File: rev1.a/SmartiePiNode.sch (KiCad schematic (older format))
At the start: 53 parts, among them CN1 USBMICROb, CN2 ST-LINK, CN3 SX1238_TRX_HEADER, SW1 SW_PUSH, U1 ISL91127IR, U2 STM32L052_LQFP48, X1 abm10, X2 ABS25-32.768KHZ-6-T

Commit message: more schematic/usb verification.
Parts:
- added R?: 1.5K, symbol R_Small
- added R?: 100K, Resistors_SMD:R_0603, symbol R_Small
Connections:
- net +3V3: now also R?.1
- net GND: now also R?.1
- net at CN1.3 (D+), R3.2: now also R?.2
- net at CN1.4 (NC): now also R?.2
- no-connect marks 3 -> 2
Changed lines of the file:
@@
 $EndComp
 $Comp
-L GND #PWR10
+L GND #PWR01
 U 1 1 5B041A53
 P 3720 7315
-F 0 "#PWR10" H 3720 7065 50  0001 C CNN
+F 0 "#PWR01" H 3720 7065 50  0001 C CNN
 F 1 "GND" H 3725 7142 50  0000 C CNN
 F 2 "" H 3720 7315 50  0001 C CNN
@@
 $EndComp
 $Comp
-L GND #PWR15
+L GND #PWR02
 U 1 1 5B041F18
 P 4975 6485
-F 0 "#PWR15" H 4975 6235 50  0001 C CNN
+F 0 "#PWR02" H 4975 6235 50  0001 C CNN
 F 1 "GND" H 4980 6312 50  0000 C CNN
 F 2 "" H 4975 6485 50  0001 C CNN
@@
 $EndComp
 $Comp
-L GND #PWR16
+L GND #PWR03
 U 1 1 5B04234F
 P 5255 6485
-F 0 "#PWR16" H 5255 6235 50  0001 C CNN
+F 0 "#PWR03" H 5255 6235 50  0001 C CNN
 F 1 "GND" H 5260 6312 50  0000 C CNN
 F 2 "" H 5255 6485 50  0001 C CNN
@@
 $EndComp
 $Comp
-L GND #PWR17
+L GND #PWR04
 U 1 1 5B0423C8
 P 5530 6485
-F 0 "#PWR17" H 5530 6235 50  0001 C CNN
+F 0 "#PWR04" H 5530 6235 50  0001 C CNN
 F 1 "GND" H 5535 6312 50  0000 C CNN
 F 2 "" H 5530 6485 50  0001 C CNN
@@
 $EndComp
 $Comp
-L GND #PWR6
+L GND #PWR05
 U 1 1 5B04306E
 P 2340 6485
-F 0 "#PWR6" H 2340 6235 50  0001 C CNN
+F 0 "#PWR05" H 2340 6235 50  0001 C CNN
 F 1 "GND" H 2345 6312 50  0000 C CNN
 F 2 "" H 2340 6485 50  0001 C CNN
@@
 $EndComp
 $Comp
-L GND #PWR4
+L GND #PWR06
 U 1 1 5B04307C
 P 2060 6485
-F 0 "#PWR4" H 2060 6235 50  0001 C CNN
+F 0 "#PWR06" H 2060 6235 50  0001 C CNN
 F 1 "GND" H 2065 6312 50  0000 C CNN
 F 2 "" H 2060 6485 50  0001 C CNN
@@
 $EndComp
 $Comp
-L GND #PWR3
+L GND #PWR07
 U 1 1 5B04308A
 P 1785 6485
-F 0 "#PWR3" H 1785 6235 50  0001 C CNN
+F 0 "#PWR07" H 1785 6235 50  0001 C CNN
 F 1 "GND" H 1790 6312 50  0000 C CNN
 F 2 "" H 1785 6485 50  0001 C CNN
@@
 $EndComp
 $Comp
-L GND #PWR7
+L GND #PWR08
 U 1 1 5B043F5D
 P 2705 7280
-F 0 "#PWR7" H 2705 7030 50  0001 C CNN
+F 0 "#PWR08" H 2705 7030 50  0001 C CNN
 F 1 "GND" H 2710 7107 50  0000 C CNN
 F 2 "" H 2705 7280 50  0001 C CNN
@@
 $EndComp
 $Comp
-L GND #PWR12
+L GND #PWR09
 U 1 1 5B044D4C
 P 4485 7315
-F 0 "#PWR12" H 4485 7065 50  0001 C CNN
+F 0 "#PWR09" H 4485 7065 50  0001 C CNN
 F 1 "GND" H 4490 7142 50  0000 C CNN
 F 2 "" H 4485 7315 50  0001 C CNN
@@
 $EndComp
 $Comp
-L GND #PWR22
+L GND #PWR010
 U 1 1 5B06F6EF
 P 9930 3790
-F 0 "#PWR22" H 9930 3540 50  0001 C CNN
+F 0 "#PWR010" H 9930 3540 50  0001 C CNN
 F 1 "GND" H 9935 3617 50  0000 C CNN
 F 2 "" H 9930 3790 50  0001 C CNN
@@
 $EndComp
 $Comp
-L GND #PWR20
+L GND #PWR011
 U 1 1 5B0753BB
 P 6760 3380
-F 0 "#PWR20" H 6760 3130 50  0001 C CNN
+F 0 "#PWR011" H 6760 3130 50  0001 C CNN
 F 1 "GND" H 6765 3207 50  0000 C CNN
 F 2 "" H 6760 3380 50  0001 C CNN
@@
 	0    1    1    0
 $EndComp
-NoConn ~ 1465 4560
-$Comp
-L GND #PWR1
+$Comp
+L GND #PWR012
 U 1 1 5B081C3A
-P 1545 4710
-F 0 "#PWR1" H 1545 4460 50  0001 C CNN
-F 1 "GND" H 1550 4537 50  0000 C CNN
-F 2 "" H 1545 4710 50  0001 C CNN
-F 3 "" H 1545 4710 50  0001 C CNN
-	1    1545 4710
+P 1715 4725
+F 0 "#PWR012" H 1715 4475 50  0001 C CNN
+F 1 "GND" H 1720 4552 50  0000 C CNN
+F 2 "" H 1715 4725 50  0001 C CNN
+F 3 "" H 1715 4725 50  0001 C CNN
+	1    1715 4725
 	1    0    0    -1
 $EndComp
@@
 $EndComp
 $Comp
-L GND #PWR18
+L GND #PWR013
 U 1 1 5B082DC4
 P 5880 3240
-F 0 "#PWR18" H 5880 2990 50  0001 C CNN
+F 0 "#PWR013" H 5880 2990 50  0001 C CNN
 F 1 "GND" H 5885 3067 50  0000 C CNN
 F 2 "" H 5880 3240 50  0001 C CNN
@@
 	1465 4260 1895 4260
 Wire Wire Line
-	1545 4660 1545 4710
-Wire Wire Line
-	1465 4660 1545 4660
-Wire Wire Line
 	1465 4460 1850 4460
 Wire Wire Line
@@
 Connection ~ 10575 2935
 $Comp
-L GND #PWR23
+L GND #PWR014
 U 1 1 5B098D9A
 P 11070 2830
-F 0 "#PWR23" H 11070 2580 50  0001 C CNN
+F 0 "#PWR014" H 11070 2580 50  0001 C CNN
 F 1 "GND" H 11075 2657 50  0000 C CNN
 F 2 "" H 11070 2830 50  0001 C CNN
@@
 	2225 1540 2225 1670
 $Comp
-L GND #PWR5
+L GND #PWR015
 U 1 1 5B0A5E1E
 P 2225 1670
-F 0 "#PWR5" H 2225 1420 50  0001 C CNN
+F 0 "#PWR015" H 2225 1420 50  0001 C CNN
 F 1 "GND" H 2230 1497 50  0000 C CNN
 F 2 "" H 2225 1670 50  0001 C CNN
@@
 +3V3
 $Comp
-L GND #PWR8
+L GND #PWR016
 U 1 1 5B0AC996
 P 3070 1200
-F 0 "#PWR8" H 3070 950 50  0001 C CNN
+F 0 "#PWR016" H 3070 950 50  0001 C CNN
 F 1 "GND" H 3075 1027 50  0000 C CNN
 F 2 "" H 3070 1200 50  0001 C CNN
@@
 SPI2_SCK
 $Comp
-L GND #PWR9
+L GND #PWR017
 U 1 1 5B0AE690
 P 3070 1500
-F 0 "#PWR9" H 3070 1250 50  0001 C CNN
+F 0 "#PWR017" H 3070 1250 50  0001 C CNN
 F 1 "GND" H 3075 1327 50  0000 C CNN
 F 2 "" H 3070 1500 50  0001 C CNN
@@
 	4145 2100 4720 2100
 $Comp
-L GND #PWR13
+L GND #PWR018
 U 1 1 5B0AEB87
 P 4720 2100
-F 0 "#PWR13" H 4720 1850 50  0001 C CNN
+F 0 "#PWR018" H 4720 1850 50  0001 C CNN
 F 1 "GND" H 4725 1927 50  0000 C CNN
 F 2 "" H 4720 2100 50  0001 C CNN
@@
 	1625 3160 1695 3160
 $Comp
-L GND #PWR2
+L GND #PWR019
 U 1 1 5B0B10C1
 P 1695 3160
-F 0 "#PWR2" H 1695 2910 50  0001 C CNN
+F 0 "#PWR019" H 1695 2910 50  0001 C CNN
 F 1 "GND" H 1700 2987 50  0000 C CNN
 F 2 "" H 1695 3160 50  0001 C CNN
@@
 NRST
 $Comp
-L GND #PWR11
+L GND #PWR020
 U 1 1 5B0B8F14
 P 4200 3080
-F 0 "#PWR11" H 4200 2830 50  0001 C CNN
+F 0 "#PWR020" H 4200 2830 50  0001 C CNN
 F 1 "GND" H 4205 2907 50  0000 C CNN
 F 2 "" H 4200 3080 50  0001 C CNN
@@
 $EndComp
 $Comp
-L GND #PWR21
+L GND #PWR021
 U 1 1 5B0C38AE
 P 8160 5860
-F 0 "#PWR21" H 8160 5610 50  0001 C CNN
+F 0 "#PWR021" H 8160 5610 50  0001 C CNN
 F 1 "GND" H 8165 5687 50  0000 C CNN
 F 2 "" H 8160 5860 50  0001 C CNN
@@
 Connection ~ 6235 2750
 $Comp
-L GND #PWR19
+L GND #PWR022
 U 1 1 5B1AE42D
 P 6235 2785
-F 0 "#PWR19" H 6235 2535 50  0001 C CNN
+F 0 "#PWR022" H 6235 2535 50  0001 C CNN
 F 1 "GND" H 6315 2770 50  0000 C CNN
 F 2 "" H 6235 2785 50  0001 C CNN
@@
 	4855 4565 4855 5170
 $Comp
-L GND #PWR14
+L GND #PWR023
 U 1 1 5B1D46F6
 P 4855 5170
-F 0 "#PWR14" H 4855 4920 50  0001 C CNN
+F 0 "#PWR023" H 4855 4920 50  0001 C CNN
 F 1 "GND" H 4860 4997 50  0000 C CNN
 F 2 "" H 4855 5170 50  0001 C CNN
@@
 Wire Wire Line
 	2735 6750 2820 6750
+$Comp
+L R_Small R?
+U 1 1 5B23E01C
+P 1950 4555
+F 0 "R?" V 1910 4445 50  0000 C CNN
+F 1 "1.5K" V 1950 4555 50  0000 C CNN
+F 2 "" H 1950 4555 50  0001 C CNN
+F 3 "" H 1950 4555 50  0001 C CNN
+	1    1950 4555
+	0    1    1    0
+$EndComp
+Wire Wire Line
+	2050 4555 2370 4555
+Text Label 2370 4555 2    60   ~ 0
++3V3
+Wire Wire Line
+	1850 4555 1740 4555
+Wire Wire Line
+	1740 4555 1740 4460
+Connection ~ 1740 4460
+$Comp
+L R_Small R?
+U 1 1 5B23F4F9
+P 1585 4560
+F 0 "R?" V 1540 4440 50  0000 C CNN
+F 1 "100K" V 1585 4560 50  0000 C CNN
+F 2 "Resistors_SMD:R_0603" H 1585 4560 50  0001 C CNN
+F 3 "" H 1585 4560 50  0001 C CNN
+	1    1585 4560
+	0    1    1    0
+$EndComp
+Wire Wire Line
+	1465 4560 1485 4560
+Wire Wire Line
+	1715 4725 1715 4560
+Wire Wire Line
+	1715 4560 1685 4560
+Wire Wire Line
+	1465 4660 1715 4660
+Connection ~ 1715 4660
 $EndSCHEMATC

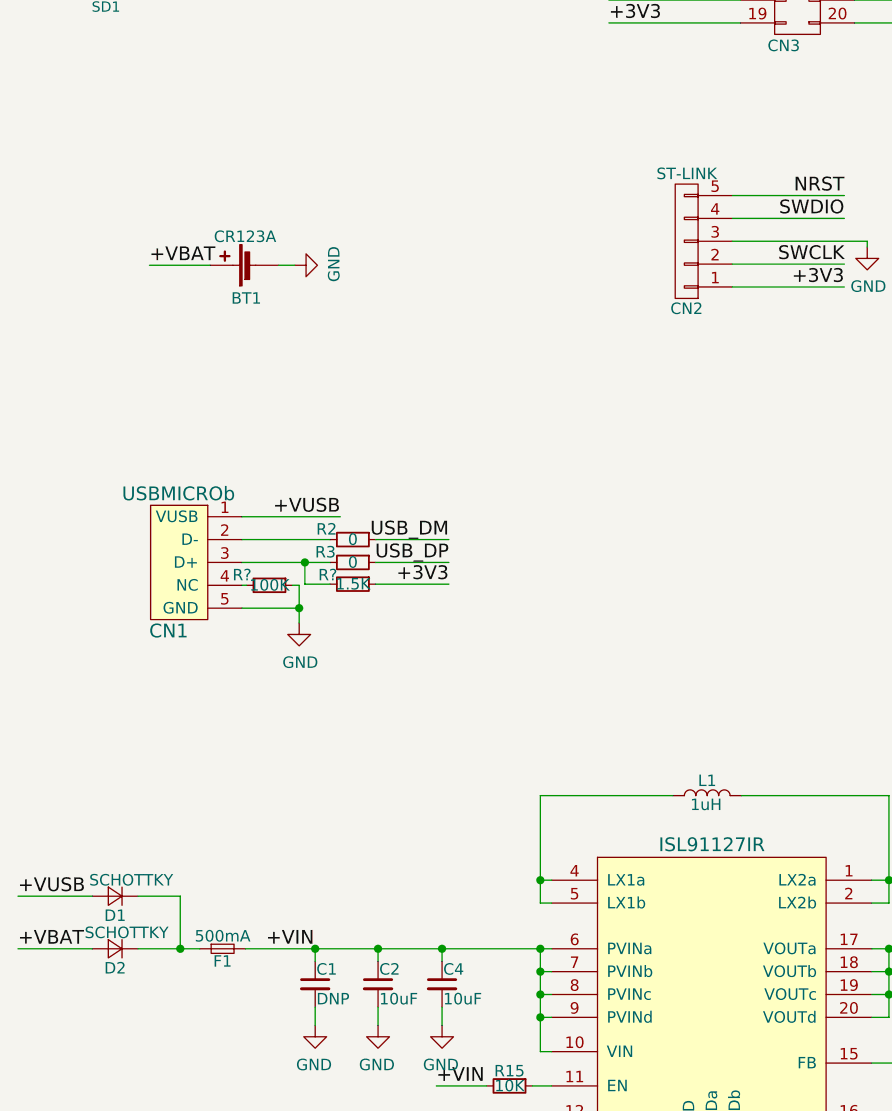
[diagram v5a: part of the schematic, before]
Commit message: footprint placement and tweaking continued...
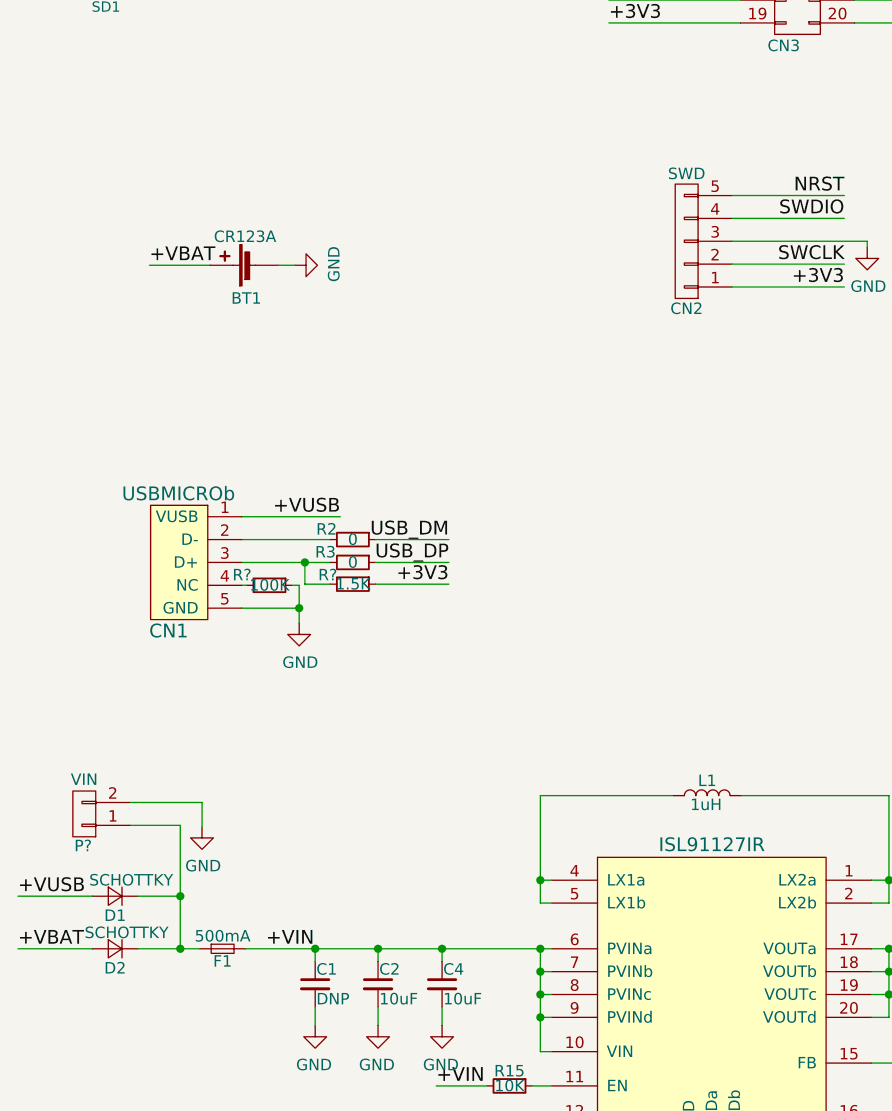
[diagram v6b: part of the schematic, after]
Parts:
- added P?: VIN, symbol CONN_01X02
- CN2: value ST-LINK -> SWD
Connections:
- net GND: now also P?.2 (P2)
- net at D1.1 (K), D2.1 (K), F1.1: now also P?.1 (P1)
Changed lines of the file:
@@
 +VBAT
 Wire Wire Line
-	1195 5920 1195 6150
+	1195 5610 1195 6150
 Connection ~ 1195 6150
 Text Label 485  5920 0    60   ~ 0
@@
 P 3410 3055
 F 0 "CN2" H 3410 3350 50  0000 C CNN
-F 1 "ST-LINK" H 3410 2760 50  0000 C CNN
+F 1 "SWD" H 3410 2760 50  0000 C CNN
 F 2 "Pin_Headers:Pin_Header_Straight_1x05" H 3410 3055 50  0001 C CNN
 F 3 "" H 3410 3055 50  0001 C CNN
@@
 	1465 4660 1715 4660
 Connection ~ 1715 4660
+$Comp
+L CONN_01X02 P?
+U 1 1 5B245A2C
+P 775 5560
+F 0 "P?" H 780 5700 50  0000 C CNN
+F 1 "VIN" H 775 5410 50  0000 C CNN
+F 2 "" H 775 5560 50  0001 C CNN
+F 3 "" H 775 5560 50  0001 C CNN
+	1    775  5560
+	-1   0    0    1
+$EndComp
+Wire Wire Line
+	975  5610 1195 5610
+Connection ~ 1195 5920
+Wire Wire Line
+	975  5510 1290 5510
+Wire Wire Line
+	1290 5510 1290 5615
+$Comp
+L GND #PWR?
+U 1 1 5B2467F2
+P 1290 5615
+F 0 "#PWR?" H 1290 5365 50  0001 C CNN
+F 1 "GND" H 1295 5442 50  0000 C CNN
+F 2 "" H 1290 5615 50  0001 C CNN
+F 3 "" H 1290 5615 50  0001 C CNN
+	1    1290 5615
+	1    0    0    -1
+$EndComp
 $EndSCHEMATC

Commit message: usb and schematic changes/tweaks.
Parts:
- added R?: DNP, symbol R_Small
- CN4: renamed from P?; footprint (none) -> Pin_Headers:Pin_Header_Straight_1x02
- R17: renamed from R?; footprint (none) -> Resistors_SMD:R_0603
- gave numbers to parts that had none: 1
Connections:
- net +3V3: now also R?.1; no longer R17.1
- net at CN1.3 (D+), R17.2, R3.2: now also R?.2
- new net USB_RENUMn: R17.1
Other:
- note removed: "second stage output filter goes here."
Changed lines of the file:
@@
 Text Notes 1590 7070 0    39   ~ 0
 MODE:\nWHEN HIGH = AUTO PFM\nWHEN LOW = FORCED PWM
-Text Notes 5500 5950 0    39   ~ 0
-second stage output filter goes here.
 $Comp
 L abracon-abm10 X1
@@
 	2735 6750 2820 6750
 $Comp
-L R_Small R?
+L R_Small R17
 U 1 1 5B23E01C
 P 1950 4555
-F 0 "R?" V 1910 4445 50  0000 C CNN
+F 0 "R17" V 1910 4445 50  0000 C CNN
 F 1 "1.5K" V 1950 4555 50  0000 C CNN
-F 2 "" H 1950 4555 50  0001 C CNN
+F 2 "Resistors_SMD:R_0603" H 1950 4555 50  0001 C CNN
 F 3 "" H 1950 4555 50  0001 C CNN
 	1    1950 4555
@@
 $EndComp
 Wire Wire Line
-	2050 4555 2370 4555
-Text Label 2370 4555 2    60   ~ 0
-+3V3
+	2050 4555 2625 4555
+Text Label 2625 4555 2    60   ~ 0
+USB_RENUMn
 Wire Wire Line
 	1850 4555 1740 4555
 Wire Wire Line
-	1740 4555 1740 4460
+	1740 4460 1740 4660
 Connection ~ 1740 4460
 $Comp
-L R_Small R?
+L R_Small R16
 U 1 1 5B23F4F9
 P 1585 4560
-F 0 "R?" V 1540 4440 50  0000 C CNN
+F 0 "R16" V 1525 4560 50  0000 C CNN
 F 1 "100K" V 1585 4560 50  0000 C CNN
 F 2 "Resistors_SMD:R_0603" H 1585 4560 50  0001 C CNN
@@
 Connection ~ 1715 4660
 $Comp
-L CONN_01X02 P?
+L CONN_01X02 CN4
 U 1 1 5B245A2C
 P 775 5560
-F 0 "P?" H 780 5700 50  0000 C CNN
+F 0 "CN4" H 780 5700 50  0000 C CNN
 F 1 "VIN" H 775 5410 50  0000 C CNN
-F 2 "" H 775 5560 50  0001 C CNN
+F 2 "Pin_Headers:Pin_Header_Straight_1x02" H 775 5560 50  0001 C CNN
 F 3 "" H 775 5560 50  0001 C CNN
 	1    775  5560
@@
 	1290 5510 1290 5615
 $Comp
-L GND #PWR?
+L GND #PWR024
 U 1 1 5B2467F2
 P 1290 5615
-F 0 "#PWR?" H 1290 5365 50  0001 C CNN
+F 0 "#PWR024" H 1290 5365 50  0001 C CNN
 F 1 "GND" H 1295 5442 50  0000 C CNN
 F 2 "" H 1290 5615 50  0001 C CNN
@@
 	1    0    0    -1
 $EndComp
+Wire Wire Line
+	1740 4660 1850 4660
+Connection ~ 1740 4555
+$Comp
+L R_Small R?
+U 1 1 5B272D51
+P 1950 4660
+F 0 "R?" V 1920 4520 50  0000 C CNN
+F 1 "DNP" V 1950 4660 50  0000 C CNN
+F 2 "" H 1950 4660 50  0001 C CNN
+F 3 "" H 1950 4660 50  0001 C CNN
+	1    1950 4660
+	0    1    1    0
+$EndComp
+Wire Wire Line
+	2050 4660 2370 4660
+Text Label 2370 4660 2    60   ~ 0
++3V3
 $EndSCHEMATC
